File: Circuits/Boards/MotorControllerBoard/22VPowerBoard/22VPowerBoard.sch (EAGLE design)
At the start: 59 parts, among them IC2 788TV, M1 IRFS7537PBF, M2 IRFS7537PBF, M3 IRFS7537PBF, M4 IRFS7537PBF, Q1 2N3904, Q2 2N3904, Q3 2N3904, Q4 2N3904, Q5 2N3904, Q6 2N3904, Q7 2N3904, Q8 2N3904

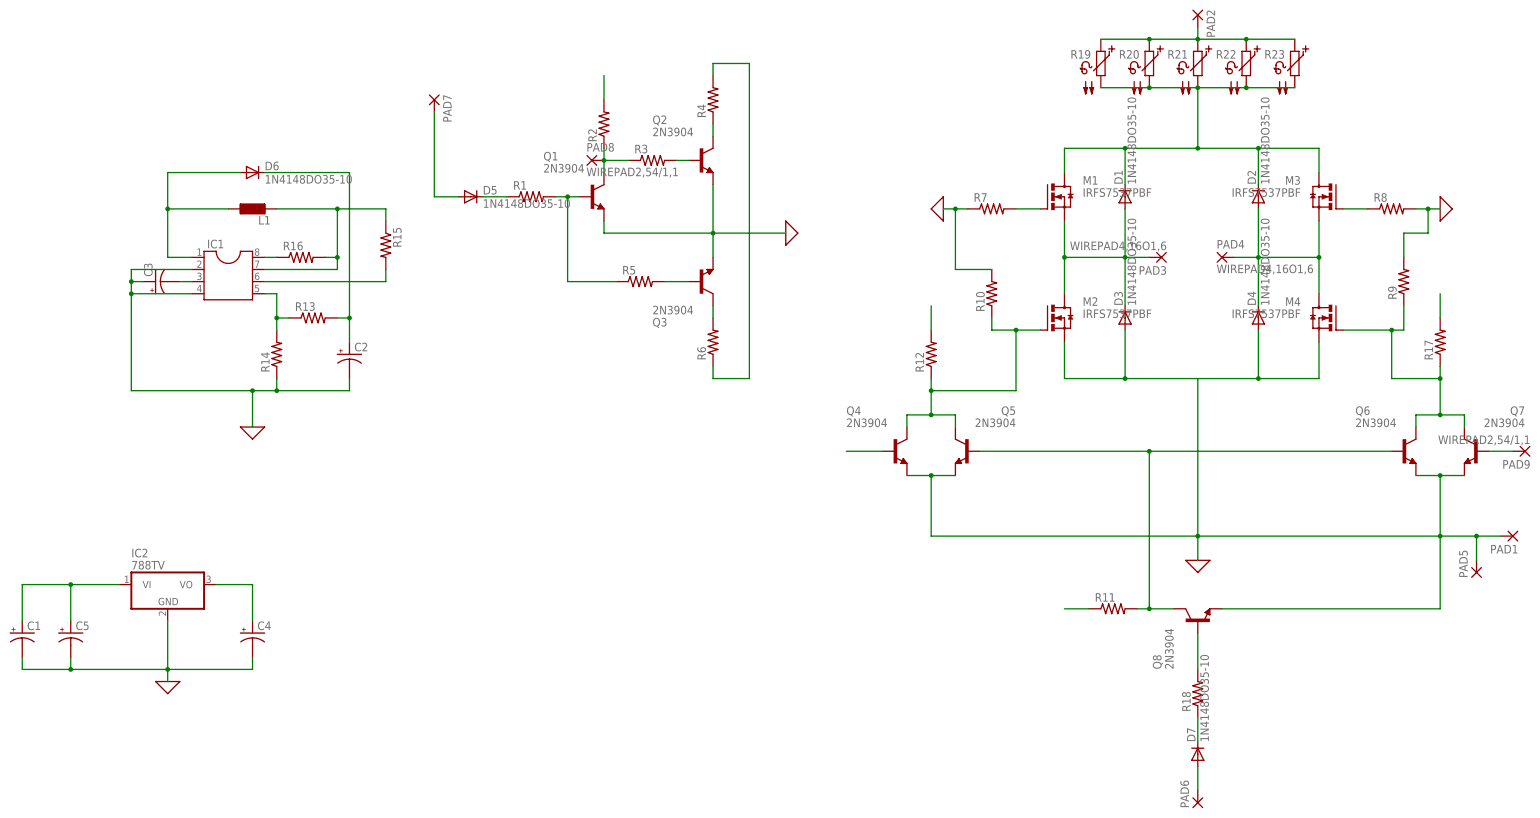
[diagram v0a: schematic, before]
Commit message: Split off 22V & 5V circuits, shrunk motor controller and began adding second to single board
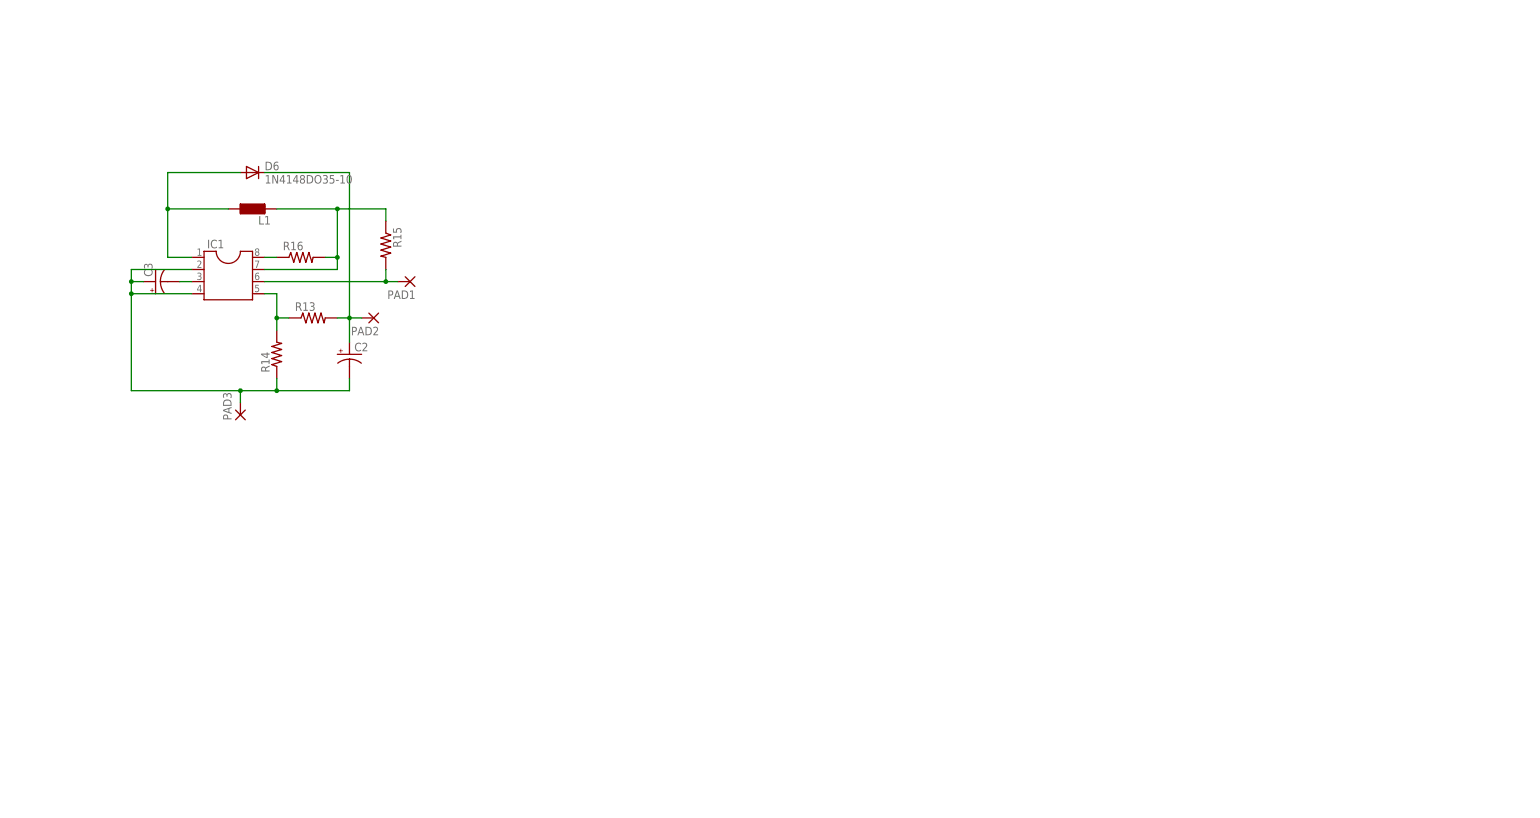
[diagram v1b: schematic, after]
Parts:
- removed C1, C4, C5: (no value), rcl:CPOL-USE2.5-7
- removed D1, D2, D3, D4, D5, D7: 1N4148DO35-10, diode:1N4148DO35-10
- removed IC2: 788TV, linear:788TV
- removed M1, M2, M3, M4: IRFS7537PBF, EagleCAD:IRFS7537PBF
- removed PAD4: WIREPAD4,16O1,6, wirepad:WIREPAD4,16O1,6
- removed PAD5: (no value), wirepad:3,81/1,4
- removed PAD6, PAD7: (no value), wirepad:2,54/1,0
- removed PAD8, PAD9: WIREPAD2,54/1,1, wirepad:WIREPAD2,54/1,1
- removed Q1, Q2, Q3, Q4, Q5, Q6, Q7, Q8: 2N3904, transistor-npn:2N3904
- removed R1, R10, R11, R12, R18, R2, R3, R4, R5, R6, R7, R8, R9: (no value), rcl:R-US_0207/7
- removed R17: (no value), resistor:R-US_0309/12
- removed R19, R20, R21, R22, R23: (no value), ptc-ntc:PTC660A
- PAD3: value WIREPAD4,16O1,6 -> (none); device wirepad:WIREPAD4,16O1,6 -> wirepad:3,81/1,4
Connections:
- removed net 0: C1.-, C2.-, C3.+, C4.-, C5.-, D3.A, D4.A, IC1.2, IC1.4, IC2.GND, M2.S, M4.S, PAD1.P, PAD5.P, Q1.E, Q2.E, Q3.E, Q4.E, Q5.E, Q6.E, Q7.E, Q8.E, R10.2, R14.1, R7.1, R8.2, R9.2
- removed net BB: Q1.B, Q4.B, R1.2, R5.1
- removed net BF: M3.G, Q3.C, R6.2, R8.1
- removed net DIR: D5.A, PAD7.P
- removed net FB: PAD8.P, Q1.C, R2.1, R3.1
- removed net FBJ: PAD9.P, Q7.B
- removed net FF: M1.G, Q2.C, R4.1, R7.2
- removed net MN: D2.A, D4.C, M3.S, M4.D, PAD4.P
- removed net MP: D1.A, D3.C, M1.S, M2.D, PAD3.P
- removed net N$16: Q5.B, Q6.B, Q8.C, R11.2
- removed net N$19: D5.C, R1.1
- removed net N$2: D7.C, R18.1
- removed net N$20: M2.G, Q4.C, Q5.C, R10.1, R12.1
- removed net N$23: Q8.B, R18.2
- removed net N$27: M4.G, Q6.C, Q7.C, R17.1, R9.1
- removed net N$3: Q2.B, R3.2
- removed net N$4: D7.A, PAD6.P
- removed net N$7: Q3.B, R5.2
- removed net VG: R4.2, R6.1
- removed net VSW: C4.+, IC2.VO, R11.1, R2.2
- net N$1: now also C2.-, C3.+, IC1.2, IC1.4, PAD3.P, R14.1; no longer PAD2.P, R19.1, R20.1, R21.1, R22.1, R23.1
- net VDD: now also PAD1.P; no longer C1.+, C5.+, D1.C, D2.C, IC2.VI, M1.D, M3.D, R12.2, R17.2, R19.2, R20.2, R21.2, R22.2, R23.2
- net VG2: now also PAD2.P
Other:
- moved on the sheet: PAD1, PAD2
